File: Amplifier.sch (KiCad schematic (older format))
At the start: 60 parts, among them J501 TB001-500-04BE CUI_Devices, Q401 2N7002, Q402 2N7002, SW501 DS04-254-2-02BK-SMT, U501 TDA7498L

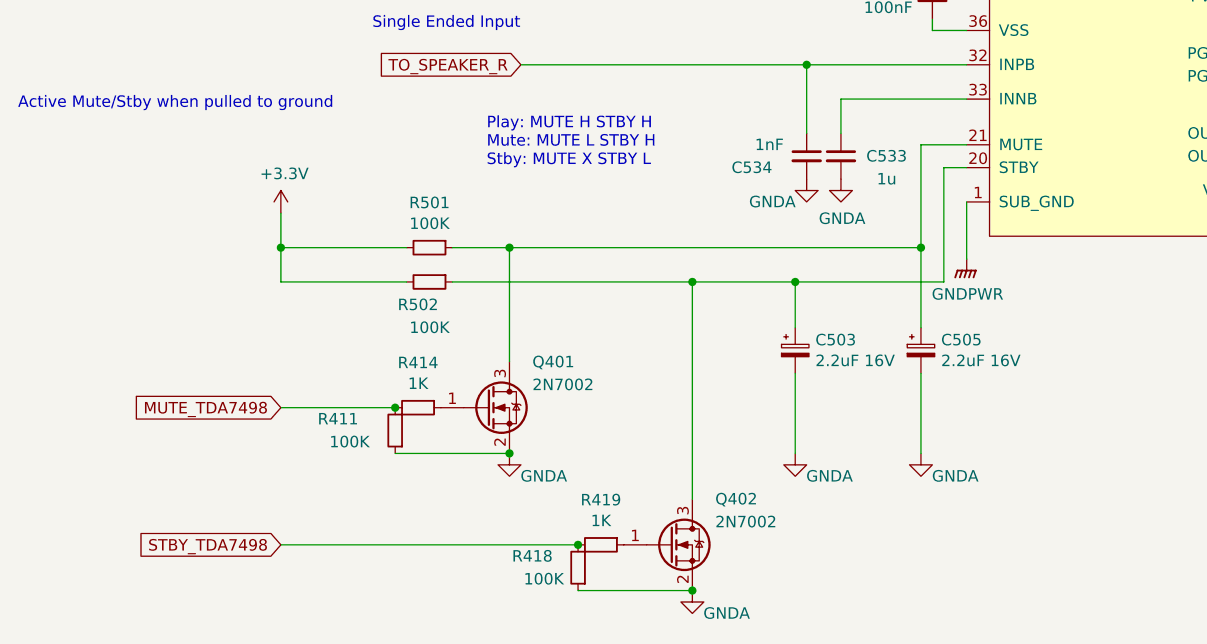
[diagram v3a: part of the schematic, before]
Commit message: Charger austauschen gegen bq24610
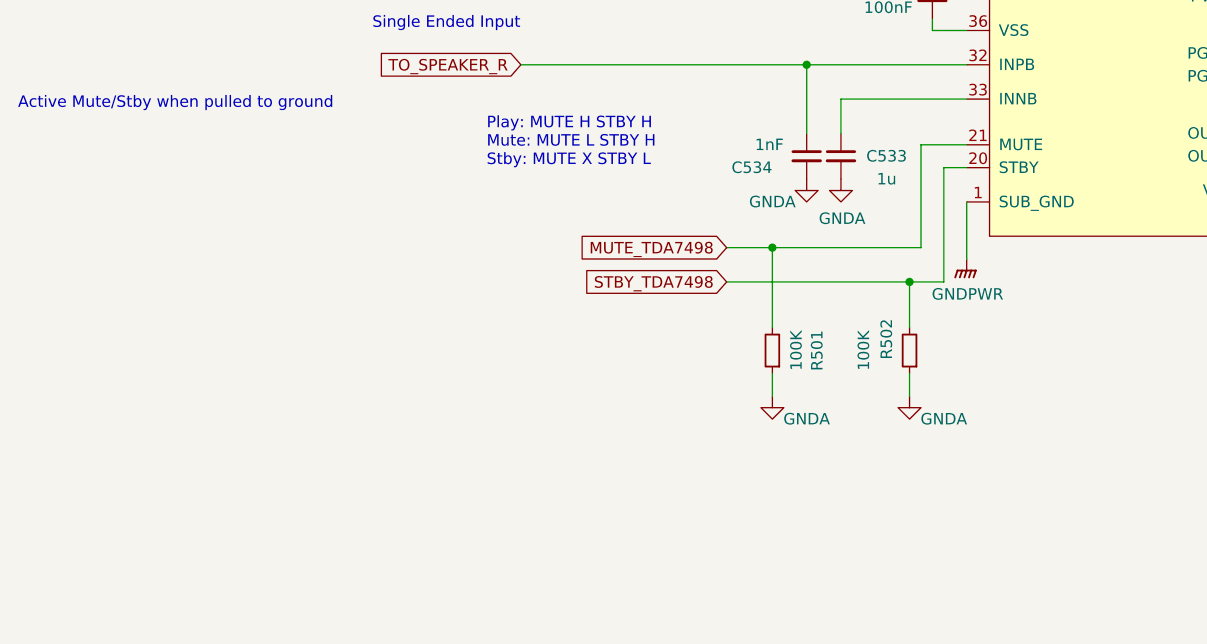
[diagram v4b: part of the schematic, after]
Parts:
- removed C503, C505: 2.2uF 16V, Capacitor_THT:CP_Radial_D4.0mm_P2.00mm, symbol Device:CP_Small
- removed Q401, Q402: 2N7002, Package_TO_SOT_SMD:SOT-23, symbol Transistor_FET:2N7002
- removed R411, R418: 100K, Resistor_SMD:R_0603_1608Metric_Pad1.05x0.95mm_HandSolder, symbol Device:R_Small
- removed R414, R419: 1K, Resistor_SMD:R_0603_1608Metric_Pad1.05x0.95mm_HandSolder, symbol Device:R_Small
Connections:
- net GNDA: now also R501.1, R502.1
- net MUTE_TDA7498: now also R501.2, U501.21 (MUTE)
- net STBY_TDA7498: now also R502.2, U501.20 (STBY)
- removed net +3V3: R501.2, R502.2
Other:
- moved on the sheet: R501, R502
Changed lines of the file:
@@
 EESchema Schematic File Version 4
-LIBS:MukkeBox-cache
-EELAYER 26 0
+EELAYER 30 0
 EELAYER END
 $Descr A4 11693 8268
@@
 	4600 4600 4600 4550
 $Comp
-L Device:CP_Small C505
-U 1 1 5E92B6ED
-P 4550 6000
-F 0 "C505" H 4638 6046 50  0000 L CNN
-F 1 "2.2uF 16V" H 4638 5955 50  0000 L CNN
-F 2 "Capacitor_THT:CP_Radial_D4.0mm_P2.00mm" H 4550 6000 50  0001 C CNN
-F 3 "~" H 4550 6000 50  0001 C CNN
-	1    4550 6000
-	1    0    0    -1
-$EndComp
-$Comp
-L Device:CP_Small C503
-U 1 1 5E92B9BD
-P 4000 6000
-F 0 "C503" H 4088 6046 50  0000 L CNN
-F 1 "2.2uF 16V" H 4088 5955 50  0000 L CNN
-F 2 "Capacitor_THT:CP_Radial_D4.0mm_P2.00mm" H 4000 6000 50  0001 C CNN
-F 3 "~" H 4000 6000 50  0001 C CNN
-	1    4000 6000
-	1    0    0    -1
-$EndComp
-$Comp
 L Device:R_Small R502
 U 1 1 5E92BB61
-P 2400 5700
-F 0 "R502" V 2500 5650 50  0000 C CNN
-F 1 "100K" V 2600 5700 50  0000 C CNN
-F 2 "Resistor_SMD:R_0603_1608Metric_Pad1.05x0.95mm_HandSolder" H 2400 5700 50  0001 C CNN
-F 3 "~" H 2400 5700 50  0001 C CNN
-	1    2400 5700
-	0    1    1    0
+P 4500 6000
+F 0 "R502" V 4600 5950 50  0000 C CNN
+F 1 "100K" V 4700 6000 50  0000 C CNN
+F 2 "Resistor_SMD:R_0603_1608Metric_Pad1.05x0.95mm_HandSolder" H 4500 6000 50  0001 C CNN
+F 3 "~" H 4500 6000 50  0001 C CNN
+	1    4500 6000
+	-1   0    0    1
 $EndComp
 $Comp
 L Device:R_Small R501
 U 1 1 5E92BC3F
-P 2400 5550
-F 0 "R501" V 2204 5550 50  0000 C CNN
-F 1 "100K" V 2295 5550 50  0000 C CNN
-F 2 "Resistor_SMD:R_0603_1608Metric_Pad1.05x0.95mm_HandSolder" H 2400 5550 50  0001 C CNN
-F 3 "~" H 2400 5550 50  0001 C CNN
-	1    2400 5550
-	0    1    1    0
+P 3900 6000
+F 0 "R501" V 3704 6000 50  0000 C CNN
+F 1 "100K" V 3795 6000 50  0000 C CNN
+F 2 "Resistor_SMD:R_0603_1608Metric_Pad1.05x0.95mm_HandSolder" H 3900 6000 50  0001 C CNN
+F 3 "~" H 3900 6000 50  0001 C CNN
+	1    3900 6000
+	-1   0    0    1
 $EndComp
 Wire Wire Line
@@
 Text Notes 4350 1000 0    89   ~ 0
 65W an 32V mit 8 Ohm Speaker
-Text GLabel 1750 6250 0    50   Input ~ 0
+Text GLabel 3700 5550 0    50   Input ~ 0
 MUTE_TDA7498
-Text GLabel 1750 6850 0    50   Input ~ 0
+Text GLabel 3700 5700 0    50   Input ~ 0
 STBY_TDA7498
 Text Notes 2650 5200 0    50   ~ 0
@@
 	1    0    0    -1
 $EndComp
-$Comp
-L power:+3.3V #PWR0401
-U 1 1 5EEBB7BD
-P 1750 5400
-F 0 "#PWR0401" H 1750 5250 50  0001 C CNN
-F 1 "+3.3V" H 1765 5573 50  0000 C CNN
-F 2 "" H 1750 5400 50  0001 C CNN
-F 3 "" H 1750 5400 50  0001 C CNN
-	1    1750 5400
-	1    0    0    -1
-$EndComp
-Wire Wire Line
-	4000 5700 4000 5900
-Wire Wire Line
-	4000 5700 4650 5700
 Wire Wire Line
 	4550 5100 4550 5550
-Wire Wire Line
-	2500 5550 2750 5550
-Connection ~ 4550 5550
-Wire Wire Line
-	4550 5550 4550 5900
-Wire Wire Line
-	4000 5700 3550 5700
-Connection ~ 4000 5700
-$Comp
-L Transistor_FET:2N7002 Q?
-U 1 1 5EF0C11E
-P 2650 6250
-AR Path="/5E73BB4A/5EF0C11E" Ref="Q?"  Part="1"
-AR Path="/5E751A81/5EF0C11E" Ref="Q401"  Part="1"
-F 0 "Q401" H 2850 6450 50  0000 L CNN
-F 1 "2N7002" H 2850 6350 50  0000 L CNN
-F 2 "Package_TO_SOT_SMD:SOT-23" H 2850 6175 50  0001 L CIN
-F 3 "https://www.fairchildsemi.com/datasheets/2N/2N7002.pdf" H 2650 6250 50  0001 L CNN
-	1    2650 6250
-	1    0    0    -1
-$EndComp
-$Comp
-L Transistor_FET:2N7002 Q?
-U 1 1 5EF1626F
-P 3450 6850
-AR Path="/5E73BB4A/5EF1626F" Ref="Q?"  Part="1"
-AR Path="/5E751A81/5EF1626F" Ref="Q402"  Part="1"
-F 0 "Q402" H 3650 7050 50  0000 L CNN
-F 1 "2N7002" H 3650 6950 50  0000 L CNN
-F 2 "Package_TO_SOT_SMD:SOT-23" H 3650 6775 50  0001 L CIN
-F 3 "https://www.fairchildsemi.com/datasheets/2N/2N7002.pdf" H 3450 6850 50  0001 L CNN
-	1    3450 6850
-	1    0    0    -1
-$EndComp
-Wire Wire Line
-	2750 6050 2750 5550
-Connection ~ 2750 5550
-Wire Wire Line
-	2750 5550 4550 5550
-Wire Wire Line
-	3550 6650 3550 5700
-Connection ~ 3550 5700
-Wire Wire Line
-	3550 5700 2500 5700
-Wire Wire Line
-	4550 6450 4550 6100
-Wire Wire Line
-	4000 6100 4000 6450
-$Comp
-L Device:R_Small R411
-U 1 1 5EF6B464
-P 2250 6350
-F 0 "R411" H 2500 6300 50  0000 C CNN
-F 1 "100K" H 2450 6400 50  0000 C CNN
-F 2 "Resistor_SMD:R_0603_1608Metric_Pad1.05x0.95mm_HandSolder" H 2250 6350 50  0001 C CNN
-F 3 "~" H 2250 6350 50  0001 C CNN
-	1    2250 6350
-	-1   0    0    1
-$EndComp
-$Comp
-L Device:R_Small R418
-U 1 1 5EF6B555
-P 3050 6950
-F 0 "R418" H 3250 6900 50  0000 C CNN
-F 1 "100K" H 3200 7000 50  0000 C CNN
-F 2 "Resistor_SMD:R_0603_1608Metric_Pad1.05x0.95mm_HandSolder" H 3050 6950 50  0001 C CNN
-F 3 "~" H 3050 6950 50  0001 C CNN
-	1    3050 6950
-	-1   0    0    1
-$EndComp
-Wire Wire Line
-	3050 7050 3550 7050
-Wire Wire Line
-	2250 6450 2750 6450
-$Comp
-L Device:R_Small R414
-U 1 1 5EF8E991
-P 2350 6250
-F 0 "R414" V 2154 6250 50  0000 C CNN
-F 1 "1K" V 2245 6250 50  0000 C CNN
-F 2 "Resistor_SMD:R_0603_1608Metric_Pad1.05x0.95mm_HandSolder" H 2350 6250 50  0001 C CNN
-F 3 "~" H 2350 6250 50  0001 C CNN
-	1    2350 6250
-	0    1    1    0
-$EndComp
-$Comp
-L Device:R_Small R419
-U 1 1 5EFB0278
-P 3150 6850
-F 0 "R419" V 2954 6850 50  0000 C CNN
-F 1 "1K" V 3045 6850 50  0000 C CNN
-F 2 "Resistor_SMD:R_0603_1608Metric_Pad1.05x0.95mm_HandSolder" H 3150 6850 50  0001 C CNN
-F 3 "~" H 3150 6850 50  0001 C CNN
-	1    3150 6850
-	0    1    1    0
-$EndComp
-Wire Wire Line
-	2250 6250 1750 6250
-Connection ~ 2250 6250
-Wire Wire Line
-	1750 6850 3050 6850
-Connection ~ 3050 6850
-Wire Wire Line
-	1750 5550 1750 5400
-Wire Wire Line
-	1750 5550 2300 5550
-Wire Wire Line
-	1750 5700 1750 5550
-Wire Wire Line
-	1750 5700 2300 5700
-Connection ~ 1750 5550
 Connection ~ 8400 3800
 Wire Wire Line
@@
 $EndComp
 $Comp
-L power:GNDA #PWR0145
-U 1 1 5ED1CFBB
-P 4550 6450
-F 0 "#PWR0145" H 4550 6200 50  0001 C CNN
-F 1 "GNDA" H 4700 6350 50  0000 C CNN
-F 2 "" H 4550 6450 50  0001 C CNN
-F 3 "" H 4550 6450 50  0001 C CNN
-	1    4550 6450
-	1    0    0    -1
-$EndComp
-$Comp
-L power:GNDA #PWR0146
-U 1 1 5ED1D0F2
-P 4000 6450
-F 0 "#PWR0146" H 4000 6200 50  0001 C CNN
-F 1 "GNDA" H 4150 6350 50  0000 C CNN
-F 2 "" H 4000 6450 50  0001 C CNN
-F 3 "" H 4000 6450 50  0001 C CNN
-	1    4000 6450
-	1    0    0    -1
-$EndComp
-$Comp
-L power:GNDA #PWR0152
-U 1 1 5ED1D1E5
-P 2750 6450
-F 0 "#PWR0152" H 2750 6200 50  0001 C CNN
-F 1 "GNDA" H 2900 6350 50  0000 C CNN
-F 2 "" H 2750 6450 50  0001 C CNN
-F 3 "" H 2750 6450 50  0001 C CNN
-	1    2750 6450
-	1    0    0    -1
-$EndComp
-$Comp
 L power:GNDA #PWR0153
 U 1 1 5ED1D264
-P 3550 7050
-F 0 "#PWR0153" H 3550 6800 50  0001 C CNN
-F 1 "GNDA" H 3700 6950 50  0000 C CNN
-F 2 "" H 3550 7050 50  0001 C CNN
-F 3 "" H 3550 7050 50  0001 C CNN
-	1    3550 7050
-	1    0    0    -1
-$EndComp
-Connection ~ 2750 6450
-Connection ~ 3550 7050
+P 4500 6200
+F 0 "#PWR0153" H 4500 5950 50  0001 C CNN
+F 1 "GNDA" H 4650 6100 50  0000 C CNN
+F 2 "" H 4500 6200 50  0001 C CNN
+F 3 "" H 4500 6200 50  0001 C CNN
+	1    4500 6200
+	1    0    0    -1
+$EndComp
 $Comp
 L Device:R_Small R5
@@
 Wire Wire Line
 	7850 3900 7850 3800
+$Comp
+L power:GNDA #PWR0401
+U 1 1 5ED8E676
+P 3900 6200
+F 0 "#PWR0401" H 3900 5950 50  0001 C CNN
+F 1 "GNDA" H 4050 6100 50  0000 C CNN
+F 2 "" H 3900 6200 50  0001 C CNN
+F 3 "" H 3900 6200 50  0001 C CNN
+	1    3900 6200
+	1    0    0    -1
+$EndComp
+Wire Wire Line
+	3700 5700 4500 5700
+Wire Wire Line
+	3700 5550 3900 5550
+Wire Wire Line
+	3900 5900 3900 5550
+Connection ~ 3900 5550
+Wire Wire Line
+	3900 5550 4550 5550
+Wire Wire Line
+	4500 5700 4500 5900
+Connection ~ 4500 5700
+Wire Wire Line
+	4500 5700 4650 5700
+Wire Wire Line
+	4500 6100 4500 6200
+Wire Wire Line
+	3900 6100 3900 6200
 $EndSCHEMATC
